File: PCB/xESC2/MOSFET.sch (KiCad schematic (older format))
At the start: 8 parts, among them Q1 BSC026N08NS5, Q2 BSC026N08NS5

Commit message: power schematic wip
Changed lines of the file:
@@
 $Descr A4 11693 8268
 encoding utf-8
-Sheet 4 5
+Sheet 3 5
 Title ""
 Date ""
@@
 AR Path="/61A3D65E/61A57DD0/61A3DBC1" Ref="Q3"  Part="1"
 AR Path="/61A3D65E/61A580D2/61A3DBC1" Ref="Q5"  Part="1"
-F 0 "Q3" H 7054 2846 50  0000 L CNN
+AR Path="/61A3F4E8/61A3D6CE/61A3DBC1" Ref="Q1"  Part="1"
+AR Path="/61A3F4E8/61A57DD0/61A3DBC1" Ref="Q3"  Part="1"
+AR Path="/61A3F4E8/61A580D2/61A3DBC1" Ref="Q5"  Part="1"
+F 0 "Q5" H 7054 2846 50  0000 L CNN
 F 1 "BSC026N08NS5" H 7054 2755 50  0000 L CNN
 F 2 "Package_TO_SOT_SMD:TDSON-8-1" H 7050 2725 50  0001 L CIN
@@
 AR Path="/61A3D65E/61A57DD0/61A49E65" Ref="Q4"  Part="1"
 AR Path="/61A3D65E/61A580D2/61A49E65" Ref="Q6"  Part="1"
-F 0 "Q4" H 7054 3846 50  0000 L CNN
+AR Path="/61A3F4E8/61A3D6CE/61A49E65" Ref="Q2"  Part="1"
+AR Path="/61A3F4E8/61A57DD0/61A49E65" Ref="Q4"  Part="1"
+AR Path="/61A3F4E8/61A580D2/61A49E65" Ref="Q6"  Part="1"
+F 0 "Q6" H 7054 3846 50  0000 L CNN
 F 1 "BSC026N08NS5" H 7054 3755 50  0000 L CNN
 F 2 "Package_TO_SOT_SMD:TDSON-8-1" H 7050 3725 50  0001 L CIN
@@
 AR Path="/61A3D65E/61A57DD0/61A4A6DC" Ref="R7"  Part="1"
 AR Path="/61A3D65E/61A580D2/61A4A6DC" Ref="R11"  Part="1"
-F 0 "R7" V 7493 3300 50  0000 C CNN
+AR Path="/61A3F4E8/61A3D6CE/61A4A6DC" Ref="R3"  Part="1"
+AR Path="/61A3F4E8/61A57DD0/61A4A6DC" Ref="R7"  Part="1"
+AR Path="/61A3F4E8/61A580D2/61A4A6DC" Ref="R11"  Part="1"
+F 0 "R11" V 7493 3300 50  0000 C CNN
 F 1 "R" V 7584 3300 50  0000 C CNN
 F 2 "Resistor_SMD:R_2512_6332Metric" V 7630 3300 50  0001 C CNN
@@
 AR Path="/61A3D65E/61A57DD0/61A4C174" Ref="R5"  Part="1"
 AR Path="/61A3D65E/61A580D2/61A4C174" Ref="R9"  Part="1"
-F 0 "R5" V 5843 2800 50  0000 C CNN
+AR Path="/61A3F4E8/61A3D6CE/61A4C174" Ref="R1"  Part="1"
+AR Path="/61A3F4E8/61A57DD0/61A4C174" Ref="R5"  Part="1"
+AR Path="/61A3F4E8/61A580D2/61A4C174" Ref="R9"  Part="1"
+F 0 "R9" V 5843 2800 50  0000 C CNN
 F 1 "2R2" V 5934 2800 50  0000 C CNN
 F 2 "Resistor_SMD:R_0603_1608Metric" V 5980 2800 50  0001 C CNN
@@
 AR Path="/61A3D65E/61A57DD0/61A4E336" Ref="R6"  Part="1"
 AR Path="/61A3D65E/61A580D2/61A4E336" Ref="R10"  Part="1"
-F 0 "R6" V 5843 3800 50  0000 C CNN
+AR Path="/61A3F4E8/61A3D6CE/61A4E336" Ref="R2"  Part="1"
+AR Path="/61A3F4E8/61A57DD0/61A4E336" Ref="R6"  Part="1"
+AR Path="/61A3F4E8/61A580D2/61A4E336" Ref="R10"  Part="1"
+F 0 "R10" V 5843 3800 50  0000 C CNN
 F 1 "2R2" V 5934 3800 50  0000 C CNN
 F 2 "Resistor_SMD:R_0603_1608Metric" V 5980 3800 50  0001 C CNN
@@
 AR Path="/61A3D65E/61A57DD0/61A4F365" Ref="TP2"  Part="1"
 AR Path="/61A3D65E/61A580D2/61A4F365" Ref="TP3"  Part="1"
-F 0 "TP2" V 8304 3488 50  0000 L CNN
+AR Path="/61A3F4E8/61A3D6CE/61A4F365" Ref="TP1"  Part="1"
+AR Path="/61A3F4E8/61A57DD0/61A4F365" Ref="TP2"  Part="1"
+AR Path="/61A3F4E8/61A580D2/61A4F365" Ref="TP3"  Part="1"
+F 0 "TP3" V 8304 3488 50  0000 L CNN
 F 1 "TestPoint" V 8395 3488 50  0000 L CNN
 F 2 "TestPoint:TestPoint_Pad_4.0x4.0mm" H 8550 3300 50  0001 C CNN
@@
 AR Path="/61A3D65E/61A57DD0/61A51593" Ref="R8"  Part="1"
 AR Path="/61A3D65E/61A580D2/61A51593" Ref="R12"  Part="1"
-F 0 "R8" H 8170 4046 50  0000 L CNN
+AR Path="/61A3F4E8/61A3D6CE/61A51593" Ref="R4"  Part="1"
+AR Path="/61A3F4E8/61A57DD0/61A51593" Ref="R8"  Part="1"
+AR Path="/61A3F4E8/61A580D2/61A51593" Ref="R12"  Part="1"
+F 0 "R12" H 8170 4046 50  0000 L CNN
 F 1 "10R" H 8170 3955 50  0000 L CNN
 F 2 "Resistor_SMD:R_0603_1608Metric" V 8030 4000 50  0001 C CNN
@@
 AR Path="/61A3D65E/61A57DD0/61A525E2" Ref="#PWR0103"  Part="1"
 AR Path="/61A3D65E/61A580D2/61A525E2" Ref="#PWR0105"  Part="1"
-F 0 "#PWR0103" H 6950 4300 50  0001 C CNN
+AR Path="/61A3F4E8/61A3D6CE/61A525E2" Ref="#PWR0101"  Part="1"
+AR Path="/61A3F4E8/61A57DD0/61A525E2" Ref="#PWR0103"  Part="1"
+AR Path="/61A3F4E8/61A580D2/61A525E2" Ref="#PWR0105"  Part="1"
+F 0 "#PWR0105" H 6950 4300 50  0001 C CNN
 F 1 "GND" H 6955 4377 50  0000 C CNN
 F 2 "" H 6950 4550 50  0001 C CNN
@@
 AR Path="/61A3D65E/61A57DD0/61A5475A" Ref="C2"  Part="1"
 AR Path="/61A3D65E/61A580D2/61A5475A" Ref="C3"  Part="1"
-F 0 "C2" H 7615 2346 50  0000 L CNN
+AR Path="/61A3F4E8/61A3D6CE/61A5475A" Ref="C1"  Part="1"
+AR Path="/61A3F4E8/61A57DD0/61A5475A" Ref="C2"  Part="1"
+AR Path="/61A3F4E8/61A580D2/61A5475A" Ref="C3"  Part="1"
+F 0 "C3" H 7615 2346 50  0000 L CNN
 F 1 "2.2uF/50V" H 7615 2255 50  0000 L CNN
 F 2 "Capacitor_SMD:C_1206_3216Metric" H 7538 2150 50  0001 C CNN
@@
 AR Path="/61A3D65E/61A57DD0/61A55913" Ref="#PWR0104"  Part="1"
 AR Path="/61A3D65E/61A580D2/61A55913" Ref="#PWR0106"  Part="1"
-F 0 "#PWR0104" H 7500 2250 50  0001 C CNN
+AR Path="/61A3F4E8/61A3D6CE/61A55913" Ref="#PWR0102"  Part="1"
+AR Path="/61A3F4E8/61A57DD0/61A55913" Ref="#PWR0104"  Part="1"
+AR Path="/61A3F4E8/61A580D2/61A55913" Ref="#PWR0106"  Part="1"
+F 0 "#PWR0106" H 7500 2250 50  0001 C CNN
 F 1 "GND" H 7505 2327 50  0000 C CNN
 F 2 "" H 7500 2500 50  0001 C CNN

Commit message: wip
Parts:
- added C24: 1nF/100V, Capacitor_SMD:C_0603_1608Metric, symbol Device:C
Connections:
- net GND: now also C24.2
- net at R3.1, R4.1, TP1.1: now also C24.1
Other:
- moved on the sheet: TP3
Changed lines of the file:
@@
 L Connector:TestPoint TP1
 U 1 1 61A4F365
-P 8350 3300
+P 9050 3300
 AR Path="/61A3D65E/61A3D6CE/61A4F365" Ref="TP1"  Part="1"
 AR Path="/61A3D65E/61A57DD0/61A4F365" Ref="TP2"  Part="1"
@@
 AR Path="/61A3F4E8/61A57DD0/61A4F365" Ref="TP2"  Part="1"
 AR Path="/61A3F4E8/61A580D2/61A4F365" Ref="TP3"  Part="1"
-F 0 "TP3" V 8304 3488 50  0000 L CNN
-F 1 "TestPoint" V 8395 3488 50  0000 L CNN
-F 2 "TestPoint:TestPoint_Pad_4.0x4.0mm" H 8550 3300 50  0001 C CNN
-F 3 "~" H 8550 3300 50  0001 C CNN
-	1    8350 3300
+F 0 "TP3" V 9004 3488 50  0000 L CNN
+F 1 "TestPoint" V 9095 3488 50  0000 L CNN
+F 2 "TestPoint:TestPoint_Pad_4.0x4.0mm" H 9250 3300 50  0001 C CNN
+F 3 "~" H 9250 3300 50  0001 C CNN
+	1    9050 3300
 	0    1    1    0
 $EndComp
@@
 Connection ~ 8100 3300
 Wire Wire Line
-	8100 3300 8350 3300
+	8100 3300 8600 3300
 $Comp
 L Device:R R4
@@
 	7500 2100 6950 2100
 Connection ~ 6950 2100
+$Comp
+L Device:C C24
+U 1 1 61C6F871
+P 8600 4000
+AR Path="/61A3F4E8/61A3D6CE/61C6F871" Ref="C24"  Part="1"
+AR Path="/61A3F4E8/61A57DD0/61C6F871" Ref="C25"  Part="1"
+AR Path="/61A3F4E8/61A580D2/61C6F871" Ref="C26"  Part="1"
+F 0 "C26" H 8715 4046 50  0000 L CNN
+F 1 "1nF/100V" H 8715 3955 50  0000 L CNN
+F 2 "Capacitor_SMD:C_0603_1608Metric" H 8638 3850 50  0001 C CNN
+F 3 "~" H 8600 4000 50  0001 C CNN
+	1    8600 4000
+	1    0    0    -1
+$EndComp
+Wire Wire Line
+	8600 3850 8600 3300
+Connection ~ 8600 3300
+Wire Wire Line
+	8600 3300 9050 3300
+Wire Wire Line
+	8600 4150 8600 4550
+$Comp
+L power:GND #PWR?
+U 1 1 61C71BC5
+P 8600 4550
+AR Path="/61A3D65E/61A3D6CE/61C71BC5" Ref="#PWR?"  Part="1"
+AR Path="/61A3D65E/61A57DD0/61C71BC5" Ref="#PWR?"  Part="1"
+AR Path="/61A3D65E/61A580D2/61C71BC5" Ref="#PWR?"  Part="1"
+AR Path="/61A3F4E8/61A3D6CE/61C71BC5" Ref="#PWR0116"  Part="1"
+AR Path="/61A3F4E8/61A57DD0/61C71BC5" Ref="#PWR0117"  Part="1"
+AR Path="/61A3F4E8/61A580D2/61C71BC5" Ref="#PWR0118"  Part="1"
+F 0 "#PWR0118" H 8600 4300 50  0001 C CNN
+F 1 "GND" H 8605 4377 50  0000 C CNN
+F 2 "" H 8600 4550 50  0001 C CNN
+F 3 "" H 8600 4550 50  0001 C CNN
+	1    8600 4550
+	1    0    0    -1
+$EndComp
 $EndSCHEMATC

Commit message: wip power xESC2
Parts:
- TP1: footprint TestPoint:TestPoint_Pad_4.0x4.0mm -> xESC2:SolderPadHighCurrent
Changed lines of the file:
@@
 $Descr A4 11693 8268
 encoding utf-8
-Sheet 3 5
+Sheet 3 7
 Title ""
 Date ""
@@
 F 0 "TP3" V 9004 3488 50  0000 L CNN
 F 1 "TestPoint" V 9095 3488 50  0000 L CNN
-F 2 "TestPoint:TestPoint_Pad_4.0x4.0mm" H 9250 3300 50  0001 C CNN
+F 2 "xESC2:SolderPadHighCurrent" H 9250 3300 50  0001 C CNN
 F 3 "~" H 9250 3300 50  0001 C CNN
 	1    9050 3300

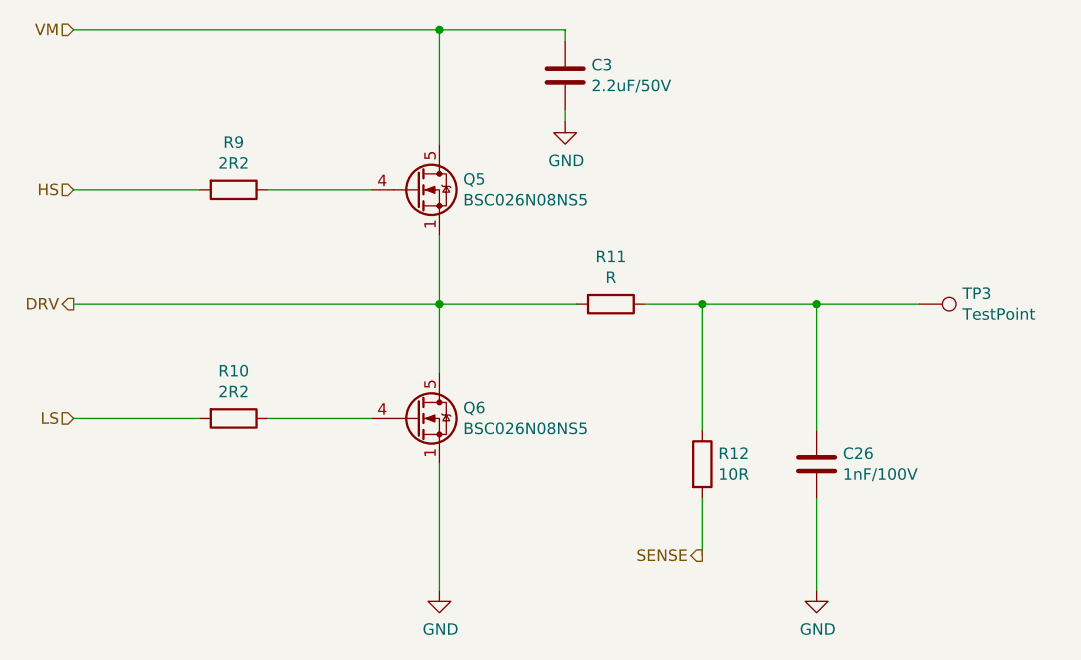
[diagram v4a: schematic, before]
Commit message: changed some values, added BOM
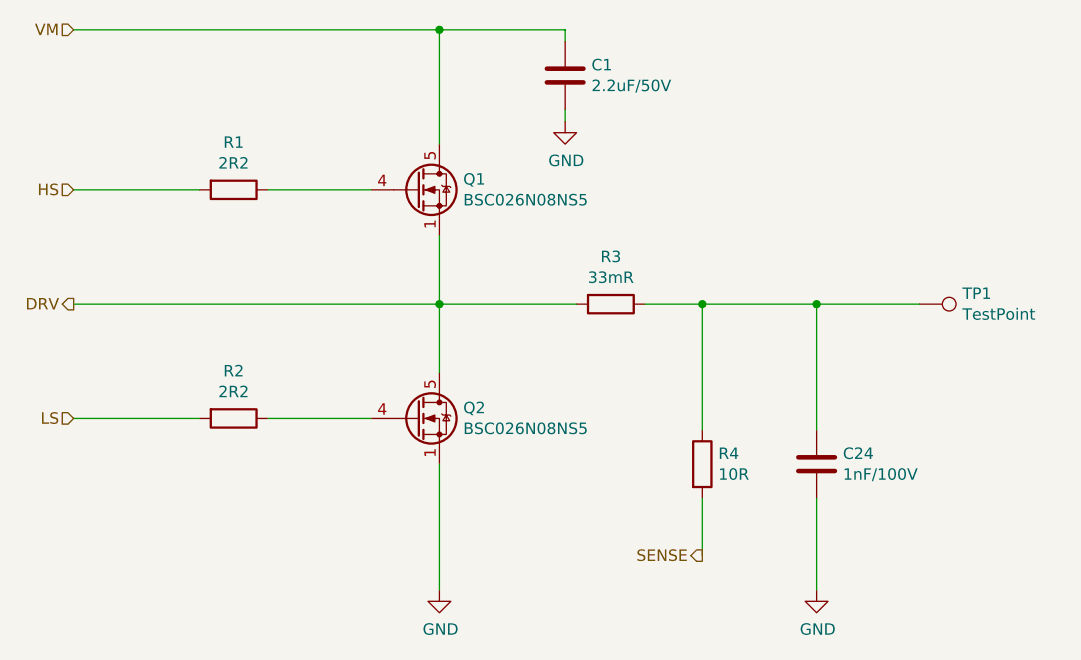
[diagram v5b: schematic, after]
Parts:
- R3: value R -> 33mR
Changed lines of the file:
@@
 $Descr A4 11693 8268
 encoding utf-8
-Sheet 5 7
+Sheet 3 7
 Title "xESC BLDC Controller"
 Date "2021-12-01"
@@
 AR Path="/61A3F4E8/61A57DD0/61A3DBC1" Ref="Q3"  Part="1"
 AR Path="/61A3F4E8/61A580D2/61A3DBC1" Ref="Q5"  Part="1"
-F 0 "Q5" H 7054 2846 50  0000 L CNN
+F 0 "Q1" H 7054 2846 50  0000 L CNN
 F 1 "BSC026N08NS5" H 7054 2755 50  0000 L CNN
 F 2 "Package_TO_SOT_SMD:TDSON-8-1" H 7050 2725 50  0001 L CIN
@@
 AR Path="/61A3F4E8/61A57DD0/61A49E65" Ref="Q4"  Part="1"
 AR Path="/61A3F4E8/61A580D2/61A49E65" Ref="Q6"  Part="1"
-F 0 "Q6" H 7054 3846 50  0000 L CNN
+F 0 "Q2" H 7054 3846 50  0000 L CNN
 F 1 "BSC026N08NS5" H 7054 3755 50  0000 L CNN
 F 2 "Package_TO_SOT_SMD:TDSON-8-1" H 7050 3725 50  0001 L CIN
@@
 AR Path="/61A3F4E8/61A57DD0/61A4A6DC" Ref="R7"  Part="1"
 AR Path="/61A3F4E8/61A580D2/61A4A6DC" Ref="R11"  Part="1"
-F 0 "R11" V 7493 3300 50  0000 C CNN
-F 1 "R" V 7584 3300 50  0000 C CNN
+F 0 "R3" V 7493 3300 50  0000 C CNN
+F 1 "33mR" V 7584 3300 50  0000 C CNN
 F 2 "Resistor_SMD:R_2512_6332Metric" V 7630 3300 50  0001 C CNN
 F 3 "~" H 7700 3300 50  0001 C CNN
@@
 AR Path="/61A3F4E8/61A57DD0/61A4C174" Ref="R5"  Part="1"
 AR Path="/61A3F4E8/61A580D2/61A4C174" Ref="R9"  Part="1"
-F 0 "R9" V 5843 2800 50  0000 C CNN
+F 0 "R1" V 5843 2800 50  0000 C CNN
 F 1 "2R2" V 5934 2800 50  0000 C CNN
 F 2 "Resistor_SMD:R_0603_1608Metric" V 5980 2800 50  0001 C CNN
@@
 AR Path="/61A3F4E8/61A57DD0/61A4E336" Ref="R6"  Part="1"
 AR Path="/61A3F4E8/61A580D2/61A4E336" Ref="R10"  Part="1"
-F 0 "R10" V 5843 3800 50  0000 C CNN
+F 0 "R2" V 5843 3800 50  0000 C CNN
 F 1 "2R2" V 5934 3800 50  0000 C CNN
 F 2 "Resistor_SMD:R_0603_1608Metric" V 5980 3800 50  0001 C CNN
@@
 AR Path="/61A3F4E8/61A57DD0/61A4F365" Ref="TP2"  Part="1"
 AR Path="/61A3F4E8/61A580D2/61A4F365" Ref="TP3"  Part="1"
-F 0 "TP3" V 9004 3488 50  0000 L CNN
+F 0 "TP1" V 9004 3488 50  0000 L CNN
 F 1 "TestPoint" V 9095 3488 50  0000 L CNN
 F 2 "xESC2:SolderPadHighCurrent" H 9250 3300 50  0001 C CNN
@@
 AR Path="/61A3F4E8/61A57DD0/61A51593" Ref="R8"  Part="1"
 AR Path="/61A3F4E8/61A580D2/61A51593" Ref="R12"  Part="1"
-F 0 "R12" H 8170 4046 50  0000 L CNN
+F 0 "R4" H 8170 4046 50  0000 L CNN
 F 1 "10R" H 8170 3955 50  0000 L CNN
 F 2 "Resistor_SMD:R_0603_1608Metric" V 8030 4000 50  0001 C CNN
@@
 AR Path="/61A3F4E8/61A57DD0/61A525E2" Ref="#PWR0103"  Part="1"
 AR Path="/61A3F4E8/61A580D2/61A525E2" Ref="#PWR0105"  Part="1"
-F 0 "#PWR0105" H 6950 4300 50  0001 C CNN
+F 0 "#PWR0101" H 6950 4300 50  0001 C CNN
 F 1 "GND" H 6955 4377 50  0000 C CNN
 F 2 "" H 6950 4550 50  0001 C CNN
@@
 AR Path="/61A3F4E8/61A57DD0/61A5475A" Ref="C2"  Part="1"
 AR Path="/61A3F4E8/61A580D2/61A5475A" Ref="C3"  Part="1"
-F 0 "C3" H 7615 2346 50  0000 L CNN
+F 0 "C1" H 7615 2346 50  0000 L CNN
 F 1 "2.2uF/50V" H 7615 2255 50  0000 L CNN
 F 2 "Capacitor_SMD:C_1206_3216Metric" H 7538 2150 50  0001 C CNN
@@
 AR Path="/61A3F4E8/61A57DD0/61A55913" Ref="#PWR0104"  Part="1"
 AR Path="/61A3F4E8/61A580D2/61A55913" Ref="#PWR0106"  Part="1"
-F 0 "#PWR0106" H 7500 2250 50  0001 C CNN
+F 0 "#PWR0102" H 7500 2250 50  0001 C CNN
 F 1 "GND" H 7505 2327 50  0000 C CNN
 F 2 "" H 7500 2500 50  0001 C CNN
@@
 AR Path="/61A3F4E8/61A57DD0/61C6F871" Ref="C25"  Part="1"
 AR Path="/61A3F4E8/61A580D2/61C6F871" Ref="C26"  Part="1"
-F 0 "C26" H 8715 4046 50  0000 L CNN
+F 0 "C24" H 8715 4046 50  0000 L CNN
 F 1 "1nF/100V" H 8715 3955 50  0000 L CNN
 F 2 "Capacitor_SMD:C_0603_1608Metric" H 8638 3850 50  0001 C CNN
@@
 AR Path="/61A3F4E8/61A57DD0/61C71BC5" Ref="#PWR0117"  Part="1"
 AR Path="/61A3F4E8/61A580D2/61C71BC5" Ref="#PWR0118"  Part="1"
-F 0 "#PWR0118" H 8600 4300 50  0001 C CNN
+F 0 "#PWR0116" H 8600 4300 50  0001 C CNN
 F 1 "GND" H 8605 4377 50  0000 C CNN
 F 2 "" H 8600 4550 50  0001 C CNN
